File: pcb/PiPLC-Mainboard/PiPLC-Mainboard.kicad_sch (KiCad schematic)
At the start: 145 parts, among them J1 WJ2EDGRC-5.08-4P, J10 WJ2EDGRC-5.08-4P, J11 WJ2EDGRC-5.08-4P, J12 WJ2EDGRC-5.08-4P, J17 Conn_02x12_Odd_Even, J2 WJ2EDGRC-5.08-4P, J3 WJ2EDGRC-5.08-4P, J4 WJ2EDGRC-5.08-4P, J5 WJ2EDGRC-5.08-4P, J6 WJ2EDGRC-5.08-4P, J7 WJ2EDGRC-5.08-4P, J8 WJ2EDGRC-5.08-4P, J9 WJ2EDGRC-5.08-4P, J99 Rpi GPIO, K1 G5RL-1A-E-TV8 DC24, K2 G5RL-1A-E-TV8 DC24, K3 G5RL-1A-E-TV8 DC24, K4 G5RL-1A-E-TV8 DC24, K5 G5RL-1A-E-TV8 DC24, K6 G5RL-1A-E-TV8 DC24, K7 G5RL-1A-E-TV8 DC24, K8 G5RL-1A-E-TV8 DC24, Q1 AO3400A, Q2 AO3400A, Q3 AO3400A, Q4 AO3400A, Q5 AO3400A, Q6 AO3400A, Q7 AO3400A, Q8 AO3400A, U1 TPS54331D, U10 EL817C, U11 EL817C, U12 ISO3082DWR, U2 NCN5121, U3 ISO1540, U4 EL817C, U5 EL817C, U6 EL817C, U7 EL817C, U8 EL817C, U9 EL817C, Y2 16MHz

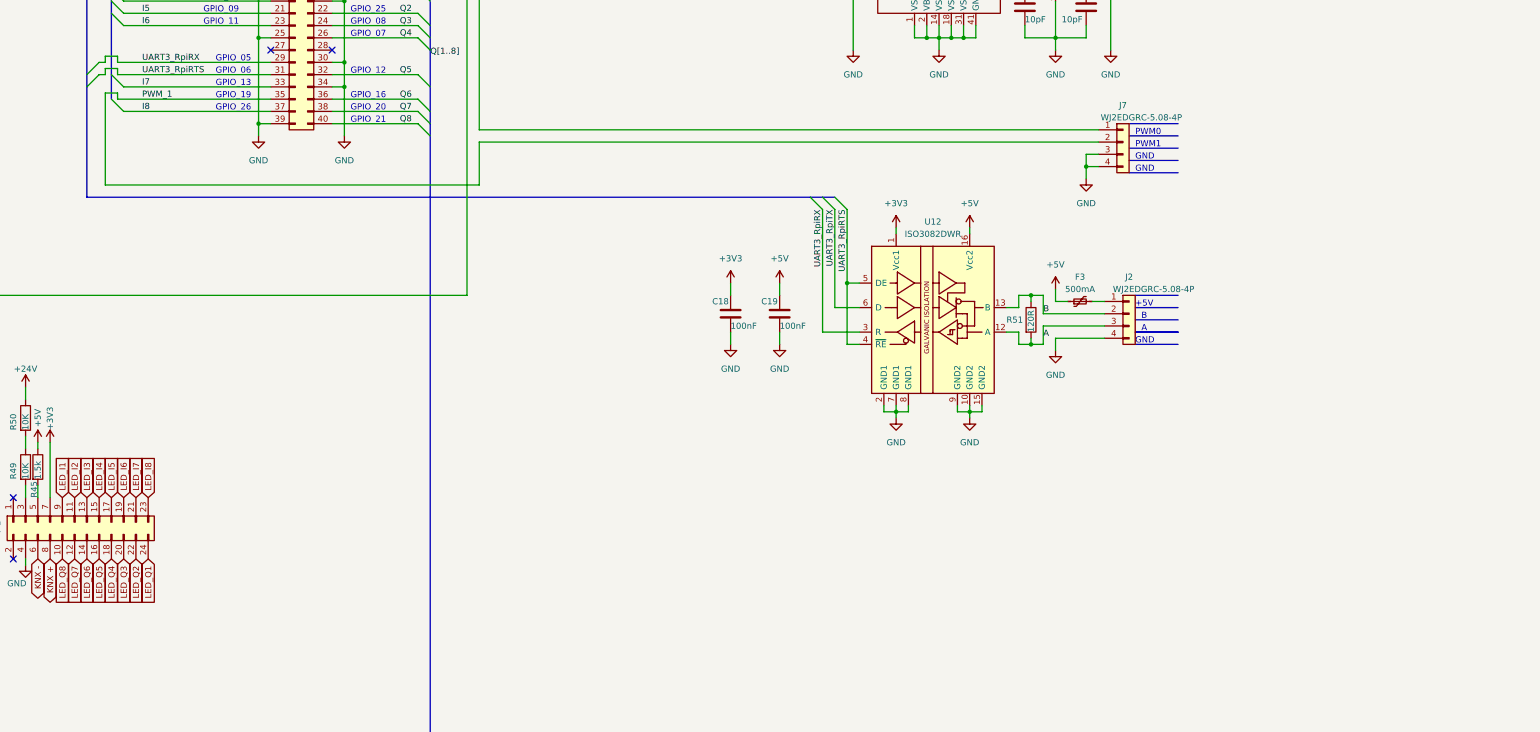
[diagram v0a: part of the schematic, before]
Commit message: [Mainboard] Add automatic DE/NRE option  for Modbus transceiver
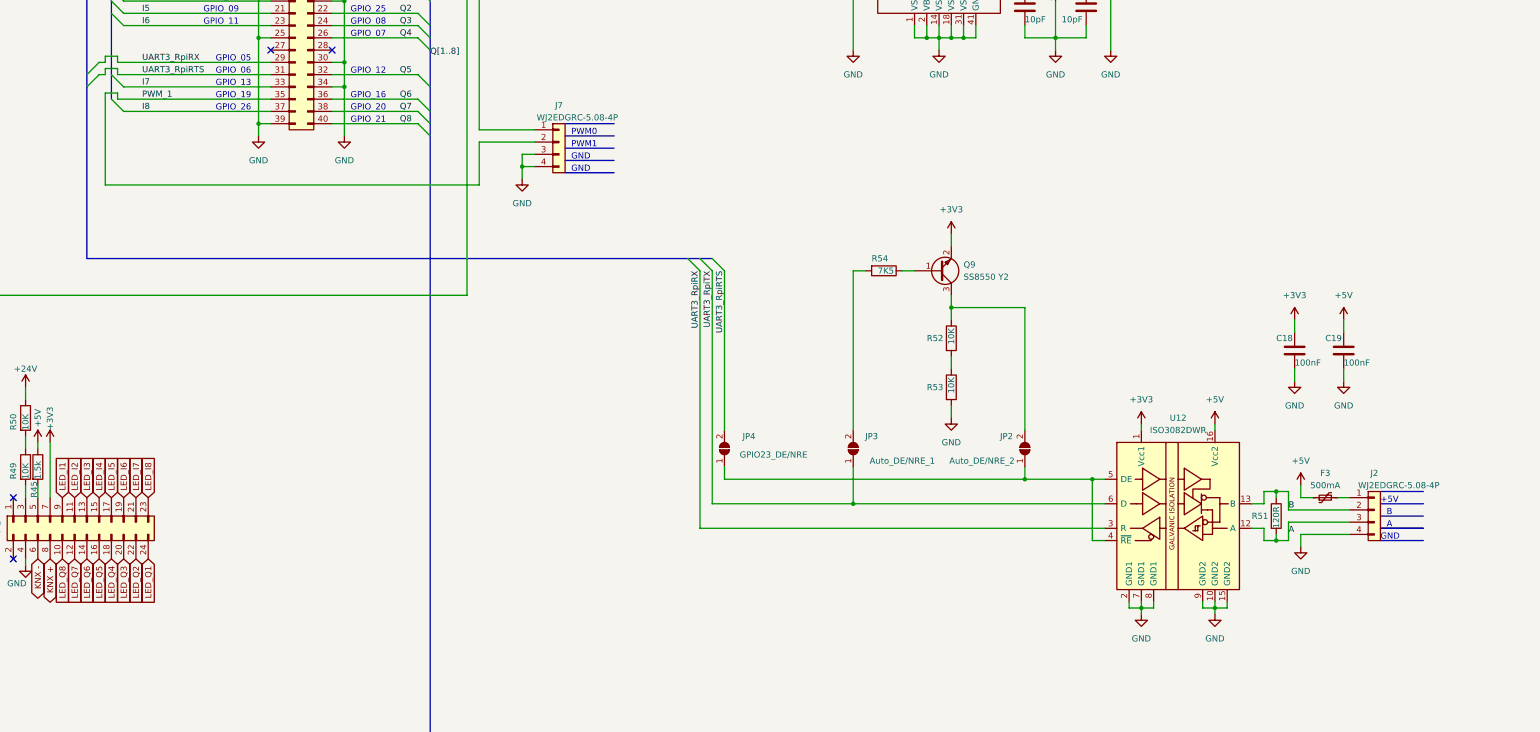
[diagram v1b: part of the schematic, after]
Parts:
- added JP2: Auto_DE/NRE_2, Jumper:SolderJumper-2_P1.3mm_Open_TrianglePad1.0x1.5mm, symbol Jumper:SolderJumper_2_Open
- added JP3: Auto_DE/NRE_1, Jumper:SolderJumper-2_P1.3mm_Open_TrianglePad1.0x1.5mm, symbol Jumper:SolderJumper_2_Open
- added JP4: GPIO23_DE/NRE, Jumper:SolderJumper-2_P1.3mm_Open_TrianglePad1.0x1.5mm, symbol Jumper:SolderJumper_2_Open
- added Q9: SS8550 Y2, Package_TO_SOT_SMD:SOT-23, symbol Device:Q_NPN_BEC
- added R52, R53: 10K, Resistor_SMD:R_0603_1608Metric, symbol Device:R
- added R54: 7K5, Resistor_SMD:R_0603_1608Metric, symbol Device:R
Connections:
- net +3V3: now also Q9.2 (E)
- net GND: now also R53.2
- net UART3_RpiRTS: now also JP4.2 (B); no longer U12.4 (~{RE}), U12.5 (DE)
- net UART3_RpiTX: now also JP3.1 (A)
- new net: JP2.1 (A), JP4.1 (A), U12.4 (~{RE}), U12.5 (DE)
- new net: R52.2, R53.1
- new net: JP3.2 (B), R54.2
- new net: JP2.2 (B), Q9.3 (C), R52.1
- new net: Q9.1 (B), R54.1
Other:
- moved on the sheet: C18, C19, F3, J2, J7, R51, U12

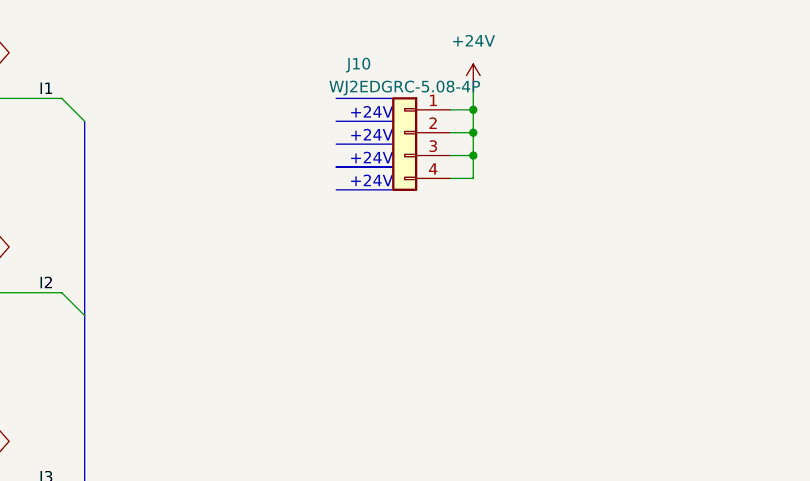
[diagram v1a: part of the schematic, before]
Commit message: [Mainboard] Add fuse to 24V DI supply
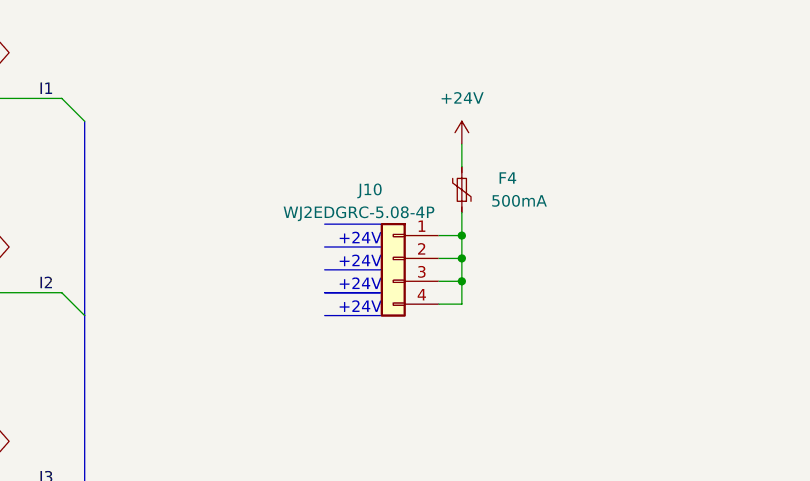
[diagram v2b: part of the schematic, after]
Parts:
- added F4: 500mA, Fuse:Fuse_0805_2012Metric, symbol Device:Polyfuse_Small
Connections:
- net +24V: now also F4.2; no longer J10.1 (Pin_1), J10.2 (Pin_2), J10.3 (Pin_3), J10.4 (Pin_4)
- new net: F4.1, J10.1 (Pin_1), J10.2 (Pin_2), J10.3 (Pin_3), J10.4 (Pin_4)
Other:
- moved on the sheet: J10
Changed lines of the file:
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@@
   (junction (at 93.98 314.96) (diameter 0) (color 0 0 0 0)
   )
-  (junction (at 243.84 34.29) (diameter 0) (color 0 0 0 0)
+  (junction (at 242.57 48.26) (diameter 0) (color 0 0 0 0)
   )
   (junction (at 154.94 297.18) (diameter 0) (color 0 0 0 0)
@@
   (junction (at 377.19 76.2) (diameter 0) (color 0 0 0 0)
   )
-  (junction (at 243.84 31.75) (diameter 0) (color 0 0 0 0)
+  (junction (at 242.57 45.72) (diameter 0) (color 0 0 0 0)
   )
   (junction (at 389.89 229.87) (diameter 0) (color 0 0 0 0)
@@
   (junction (at 231.14 138.43) (diameter 0) (color 0 0 0 0)
   )
-  (junction (at 243.84 29.21) (diameter 0) (color 0 0 0 0)
+  (junction (at 242.57 43.18) (diameter 0) (color 0 0 0 0)
   )
   (junction (at 374.65 194.31) (diameter 0) (color 0 0 0 0)
@@
     (stroke (width 0) (type default))
   )
-  (polyline (pts (xy 228.6 27.94) (xy 234.95 27.94))
+  (polyline (pts (xy 227.33 41.91) (xy 233.68 41.91))
     (stroke (width 0) (type solid))
   )
@@
     (stroke (width 0) (type default))
   )
-  (wire (pts (xy 243.84 29.21) (xy 243.84 26.67))
+  (wire (pts (xy 242.57 43.18) (xy 242.57 40.64))
     (stroke (width 0) (type default))
   )
@@
     (stroke (width 0) (type default))
   )
-  (wire (pts (xy 241.3 31.75) (xy 243.84 31.75))
+  (wire (pts (xy 240.03 45.72) (xy 242.57 45.72))
     (stroke (width 0) (type default))
   )
@@
     (stroke (width 0) (type default))
   )
-  (wire (pts (xy 241.3 29.21) (xy 243.84 29.21))
+  (wire (pts (xy 240.03 43.18) (xy 242.57 43.18))
     (stroke (width 0) (type default))
   )
@@
     (stroke (width 0) (type default))
   )
-  (polyline (pts (xy 228.6 33.02) (xy 234.95 33.02))
+  (polyline (pts (xy 227.33 46.99) (xy 233.68 46.99))
     (stroke (width 0) (type solid))
   )
@@
     (stroke (width 0) (type default))
   )
-  (polyline (pts (xy 228.6 35.56) (xy 234.95 35.56))
+  (polyline (pts (xy 227.33 49.53) (xy 233.68 49.53))
     (stroke (width 0) (type solid))
   )
@@
     (stroke (width 0) (type default))
   )
-  (wire (pts (xy 243.84 36.83) (xy 243.84 34.29))
+  (wire (pts (xy 242.57 50.8) (xy 242.57 48.26))
+    (stroke (width 0) (type default))
+  )
+  (wire (pts (xy 242.57 33.02) (xy 242.57 35.56))
     (stroke (width 0) (type default))
   )
@@
     (stroke (width 0) (type default))
   )
-  (polyline (pts (xy 228.6 38.1) (xy 234.95 38.1))
+  (polyline (pts (xy 227.33 52.07) (xy 233.68 52.07))
     (stroke (width 0) (type solid))
   )
@@
     (stroke (width 0) (type default))
   )
-  (polyline (pts (xy 228.6 30.48) (xy 234.95 30.48))
+  (polyline (pts (xy 227.33 44.45) (xy 233.68 44.45))
     (stroke (width 0) (type solid))
   )
@@
     (stroke (width 0) (type default))
   )
-  (wire (pts (xy 241.3 36.83) (xy 243.84 36.83))
+  (wire (pts (xy 240.03 50.8) (xy 242.57 50.8))
     (stroke (width 0) (type default))
   )
@@
     (stroke (width 0) (type default))
   )
-  (wire (pts (xy 243.84 31.75) (xy 243.84 29.21))
+  (wire (pts (xy 242.57 45.72) (xy 242.57 43.18))
     (stroke (width 0) (type default))
   )
@@
     (stroke (width 0) (type default))
   )
-  (wire (pts (xy 243.84 34.29) (xy 243.84 31.75))
+  (wire (pts (xy 242.57 48.26) (xy 242.57 45.72))
     (stroke (width 0) (type default))
   )
@@
     (stroke (width 0) (type default))
   )
-  (polyline (pts (xy 228.6 35.56) (xy 234.95 35.56))
+  (polyline (pts (xy 227.33 49.53) (xy 233.68 49.53))
     (stroke (width 0) (type solid))
   )
@@
     (stroke (width 0) (type default))
   )
-  (wire (pts (xy 241.3 34.29) (xy 243.84 34.29))
+  (wire (pts (xy 240.03 48.26) (xy 242.57 48.26))
     (stroke (width 0) (type default))
   )
@@
     (effects (font (size 1.27 1.27)) (justify left bottom))
   )
-  (text "+24V" (at 234.95 30.48 0)
+  (text "+24V" (at 233.68 44.45 0)
     (effects (font (size 1.27 1.27)) (justify right bottom))
   )
@@
     (effects (font (size 1.27 1.27)) (justify left bottom))
   )
-  (text "+24V" (at 234.95 38.1 0)
+  (text "+24V" (at 233.68 52.07 0)
     (effects (font (size 1.27 1.27)) (justify right bottom))
   )
@@
     (effects (font (size 1.27 1.27)) (justify left bottom))
   )
-  (text "+24V" (at 234.95 33.02 0)
+  (text "+24V" (at 233.68 46.99 0)
     (effects (font (size 1.27 1.27)) (justify right bottom))
   )
@@
     (effects (font (size 1.27 1.27)) (justify right bottom))
   )
-  (text "+24V" (at 234.95 35.56 0)
+  (text "+24V" (at 233.68 49.53 0)
     (effects (font (size 1.27 1.27)) (justify right bottom))
   )
@@
     )
   )
-  (symbol (lib_id "power:+24V") (at 243.84 26.67 0) (unit 1)
+  (symbol (lib_id "power:+24V") (at 242.57 33.02 0) (unit 1)
     (in_bom yes) (on_board yes) (dnp no) (fields_autoplaced)
-    (property "Reference" "#PWR044" (at 243.84 30.48 0)
+    (property "Reference" "#PWR044" (at 242.57 36.83 0)
       (effects (font (size 1.27 1.27)) hide)
     )
-    (property "Value" "+24V" (at 243.84 21.59 0)
+    (property "Value" "+24V" (at 242.57 27.94 0)
       (effects (font (size 1.27 1.27)))
     )
-    (property "Footprint" "" (at 243.84 26.67 0)
+    (property "Footprint" "" (at 242.57 33.02 0)
       (effects (font (size 1.27 1.27)) hide)
     )
-    (property "Datasheet" "" (at 243.84 26.67 0)
+    (property "Datasheet" "" (at 242.57 33.02 0)
       (effects (font (size 1.27 1.27)) hide)
     )
@@
     )
   )
+  (symbol (lib_id "Device:Polyfuse_Small") (at 242.57 38.1 180) (unit 1)
+    (in_bom yes) (on_board yes) (dnp no)
+    (property "Reference" "F4" (at 247.65 36.83 0)
+      (effects (font (size 1.27 1.27)))
+    )
+    (property "Value" "500mA" (at 248.92 39.37 0)
+      (effects (font (size 1.27 1.27)))
+    )
+    (property "Footprint" "Fuse:Fuse_0805_2012Metric" (at 241.3 33.02 0)
+      (effects (font (size 1.27 1.27)) (justify left) hide)
+    )
+    (property "Datasheet" "https://datasheet.lcsc.com/lcsc/2105241447_TECHFUSE-SMD0805-050-16V_C2833485.pdf" (at 242.57 38.1 0)
+      (effects (font (size 1.27 1.27)) hide)
+    )
+    (property "LCSC" "C2833485" (at 242.57 38.1 90)
+      (effects (font (size 1.27 1.27)) hide)
+    )
+    (pin "1")
+    (pin "2")
+    (instances
+      (project "PiPLC-Mainboard"
+        (path "/93ebf745-625a-4d9e-8f47-45e91f30ef94"
+          (reference "F4") (unit 1)
+        )
+      )
+    )
+  )
   (symbol (lib_id "Connector_Generic:Conn_02x12_Odd_Even") (at 193.04 238.76 90) (mirror x) (unit 1)
     (in_bom yes) (on_board yes) (dnp no)
@@
     )
   )
-  (symbol (lib_id "Connector_Generic:Conn_01x04") (at 236.22 31.75 0) (mirror y) (unit 1)
+  (symbol (lib_id "Connector_Generic:Conn_01x04") (at 234.95 45.72 0) (mirror y) (unit 1)
     (in_bom yes) (on_board yes) (dnp no)
-    (property "Reference" "J10" (at 231.14 24.13 0)
+    (property "Reference" "J10" (at 232.41 38.1 0)
       (effects (font (size 1.27 1.27)))
     )
-    (property "Value" "WJ2EDGRC-5.08-4P" (at 236.22 26.67 0)
+    (property "Value" "WJ2EDGRC-5.08-4P" (at 231.14 40.64 0)
       (effects (font (size 1.27 1.27)))
     )
-    (property "Footprint" "Connector_Phoenix_MSTB:PhoenixContact_MSTBA_2,5_4-G-5,08_1x04_P5.08mm_Horizontal" (at 236.22 31.75 0)
+    (property "Footprint" "Connector_Phoenix_MSTB:PhoenixContact_MSTBA_2,5_4-G-5,08_1x04_P5.08mm_Horizontal" (at 234.95 45.72 0)
       (effects (font (size 1.27 1.27)) hide)
     )
-    (property "Datasheet" "https://datasheet.lcsc.com/lcsc/1912251635_Ningbo-Kangnex-Elec-WJ2EDGRC-5-08-4P_C8446.pdf" (at 236.22 31.75 0)
+    (property "Datasheet" "https://datasheet.lcsc.com/lcsc/1912251635_Ningbo-Kangnex-Elec-WJ2EDGRC-5-08-4P_C8446.pdf" (at 234.95 45.72 0)
       (effects (font (size 1.27 1.27)) hide)
     )
-    (property "LCSC" "C8446" (at 236.22 31.75 0)
+    (property "LCSC" "C8446" (at 234.95 45.72 0)
       (effects (font (size 1.27 1.27)) hide)
     )

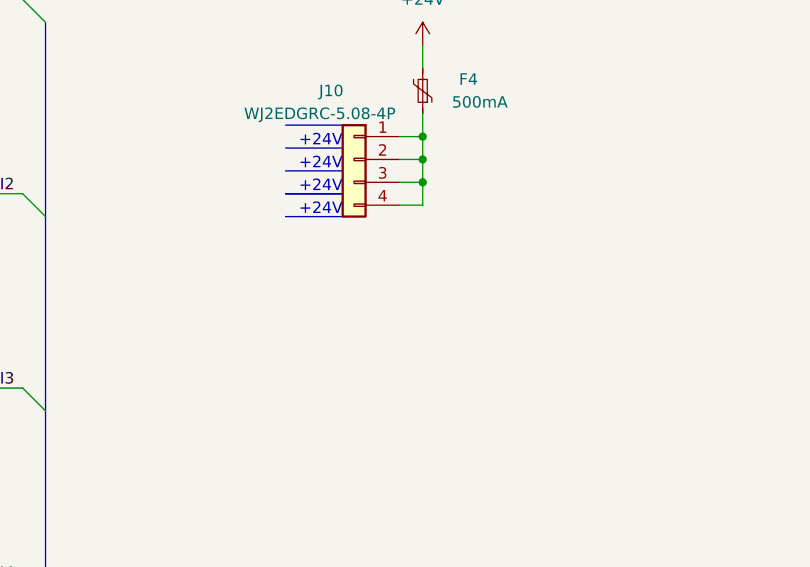
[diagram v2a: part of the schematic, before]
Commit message: [Mainboard] Decouple 24V DI supply
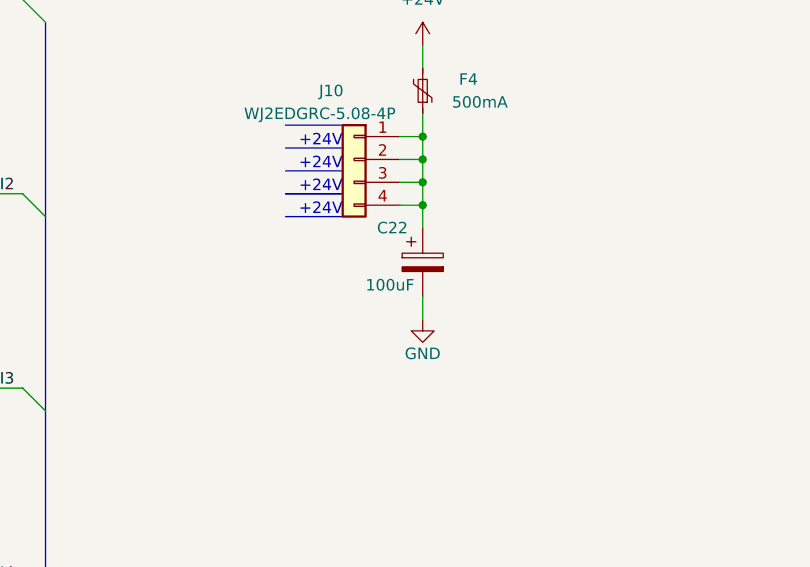
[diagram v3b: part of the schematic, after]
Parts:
- added C22: 100uF, Capacitor_SMD:CP_Elec_6.3x7.7, symbol Device:C_Polarized
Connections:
- net GND: now also C22.2
- net at F4.1, J10.1 (Pin_1), J10.2 (Pin_2)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: now also C22.1
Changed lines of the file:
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@@
   (junction (at 354.33 110.49) (diameter 0) (color 0 0 0 0)
   )
+  (junction (at 242.57 50.8) (diameter 0) (color 0 0 0 0)
+  )
   (junction (at 520.7 297.18) (diameter 0) (color 0 0 0 0)
   )
@@
     (stroke (width 0) (type default))
   )
+  (wire (pts (xy 242.57 63.5) (xy 242.57 60.96))
+    (stroke (width 0) (type default))
+  )
   (wire (pts (xy 76.2 87.63) (xy 78.74 87.63))
     (stroke (width 0) (type default))
@@
     (stroke (width 0) (type default))
   )
+  (wire (pts (xy 242.57 50.8) (xy 242.57 53.34))
+    (stroke (width 0) (type default))
+  )
   (polyline (pts (xy 20.32 26.67) (xy 26.67 26.67))
     (stroke (width 0) (type solid))
@@
     )
   )
+  (symbol (lib_id "Device:C_Polarized") (at 242.57 57.15 0) (unit 1)
+    (in_bom yes) (on_board yes) (dnp no)
+    (property "Reference" "C22" (at 237.49 53.34 0)
+      (effects (font (size 1.27 1.27)) (justify left))
+    )
+    (property "Value" "100uF" (at 236.22 59.69 0)
+      (effects (font (size 1.27 1.27)) (justify left))
+    )
+    (property "Footprint" "Capacitor_SMD:CP_Elec_6.3x7.7" (at 243.5352 60.96 0)
+      (effects (font (size 1.27 1.27)) hide)
+    )
+    (property "Datasheet" "https://datasheet.lcsc.com/lcsc/2304140030_Nichicon-UCD1V101MCL6GS_C134220.pdf" (at 242.57 57.15 0)
+      (effects (font (size 1.27 1.27)) hide)
+    )
+    (property "LCSC" "C134220" (at 242.57 57.15 0)
+      (effects (font (size 1.27 1.27)) hide)
+    )
+    (pin "1")
+    (pin "2")
+    (instances
+      (project "PiPLC-Mainboard"
+        (path "/93ebf745-625a-4d9e-8f47-45e91f30ef94"
+          (reference "C22") (unit 1)
+        )
+      )
+    )
+  )
   (symbol (lib_id "power:GND") (at 119.38 251.46 0) (unit 1)
     (in_bom yes) (on_board yes) (dnp no)
@@
         )
       )
+    )
+  )
+  (symbol (lib_id "power:GND") (at 242.57 63.5 0) (unit 1)
+    (in_bom yes) (on_board yes) (dnp no)
+    (property "Reference" "#PWR093" (at 242.57 69.85 0)
+      (effects (font (size 1.27 1.27)) hide)
+    )
+    (property "Value" "GND" (at 242.57 67.31 0)
+      (effects (font (size 1.27 1.27)))
+    )
+    (property "Footprint" "" (at 242.57 63.5 0)
+      (effects (font (size 1.27 1.27)) hide)
+    )
+    (property "Datasheet" "" (at 242.57 63.5 0)
+      (effects (font (size 1.27 1.27)) hide)
+    )
+    (pin "1")
+    (instances
+      (project "PiPLC-Mainboard"
+        (path "/93ebf745-625a-4d9e-8f47-45e91f30ef94"
+          (reference "#PWR093") (unit 1)
+        )
+      )
